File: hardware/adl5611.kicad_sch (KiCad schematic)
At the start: 6 parts, among them U18 ADL5611

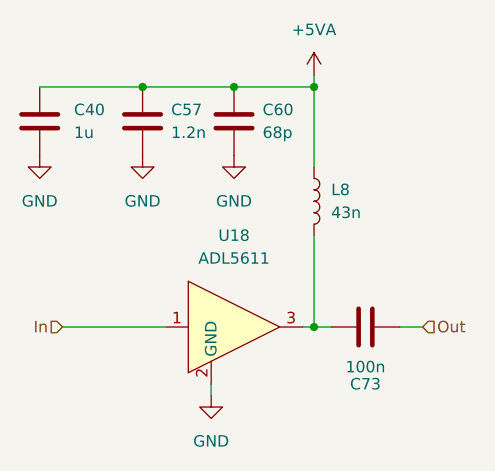
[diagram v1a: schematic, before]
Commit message: Update FEM hardware design for production version
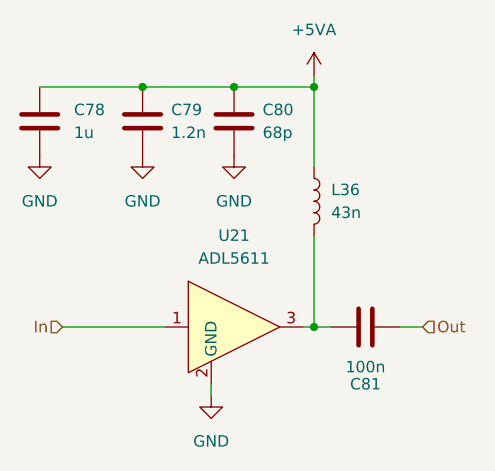
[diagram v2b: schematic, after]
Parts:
- renumbered C40 to C78, C57 to C79, C60 to C80, C73 to C81, L8 to L36, U18 to U21
